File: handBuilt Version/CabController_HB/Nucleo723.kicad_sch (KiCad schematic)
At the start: 13 parts, among them J20 TDU1, J22 CN11, J23 CN12, J24 Screw_Terminal_01x04, J25 CANbus, J26 Battery, J27 SafetyLoop, J29 TDU2, J30 TDU3, J31 TDU4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

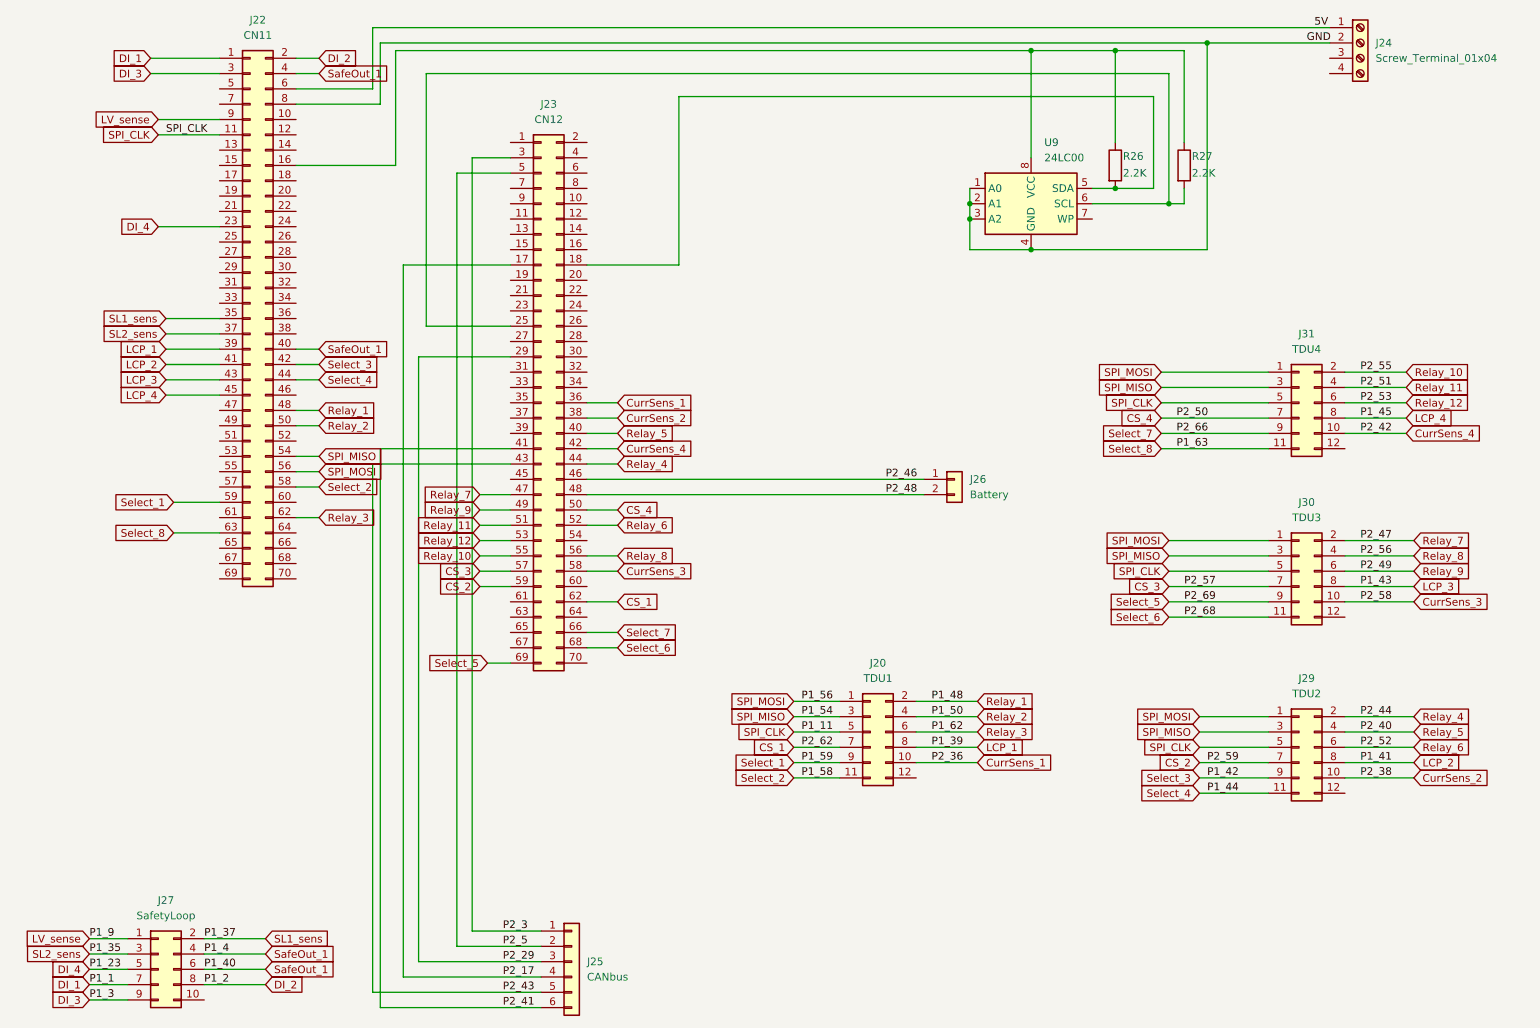
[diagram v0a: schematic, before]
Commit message: changed Connector Pinout for Nucleo
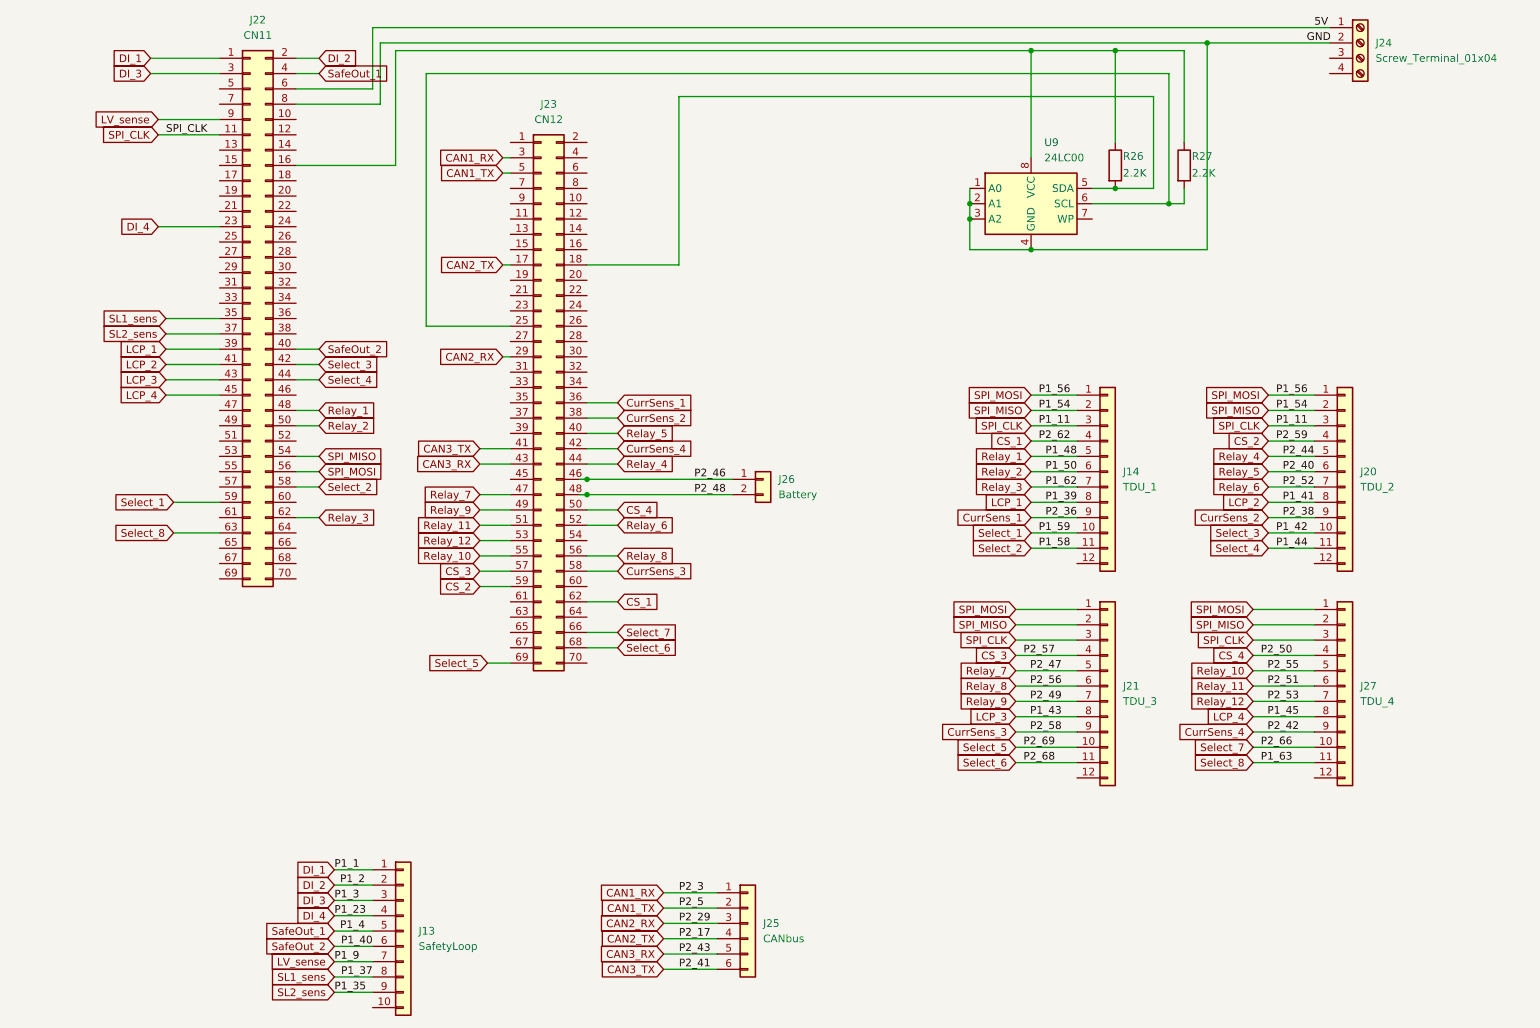
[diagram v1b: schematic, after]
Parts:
- removed J20: TDU1, symbol Connector_Generic:Conn_02x06_Odd_Even
- removed J27: SafetyLoop, symbol Connector_Generic:Conn_02x05_Odd_Even
- removed J29: TDU2, symbol Connector_Generic:Conn_02x06_Odd_Even
- removed J30: TDU3, symbol Connector_Generic:Conn_02x06_Odd_Even
- removed J31: TDU4, symbol Connector_Generic:Conn_02x06_Odd_Even
- added J13: SafetyLoop, symbol Connector_Generic:Conn_01x10
- added J14: TDU_1, symbol Connector_Generic:Conn_01x12
- added J20: TDU_2, symbol Connector_Generic:Conn_01x12
- added J21: TDU_3, symbol Connector_Generic:Conn_01x12
- added J27: TDU_4, symbol Connector_Generic:Conn_01x12
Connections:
- net CS_1: now also J14.4 (Pin_4)
- net CS_2: now also J20.4 (Pin_4)
- net CS_3: now also J21.4 (Pin_4)
- net CS_4: now also J27.4 (Pin_4)
- net CurrSens_1: now also J14.9 (Pin_9)
- net CurrSens_2: now also J20.9 (Pin_9)
- net CurrSens_3: now also J21.9 (Pin_9)
- net CurrSens_4: now also J27.9 (Pin_9)
- net DI_1: now also J13.1 (Pin_1)
- net DI_2: now also J13.2 (Pin_2)
- net DI_3: now also J13.3 (Pin_3)
- net DI_4: now also J13.4 (Pin_4)
- net LCP_1: now also J14.8 (Pin_8)
- net LCP_2: now also J20.8 (Pin_8)
- net LCP_3: now also J21.8 (Pin_8)
- net LCP_4: now also J27.8 (Pin_8)
- net LV_sense: now also J13.7 (Pin_7)
- net Relay_1: now also J14.5 (Pin_5)
- net Relay_10: now also J27.5 (Pin_5)
- net Relay_11: now also J27.6 (Pin_6)
- net Relay_12: now also J27.7 (Pin_7)
- net Relay_2: now also J14.6 (Pin_6)
- net Relay_3: now also J14.7 (Pin_7)
- net Relay_4: now also J20.5 (Pin_5)
- net Relay_5: now also J20.6 (Pin_6)
- net Relay_6: now also J20.7 (Pin_7)
- net Relay_7: now also J21.5 (Pin_5)
- net Relay_8: now also J21.6 (Pin_6)
- net Relay_9: now also J21.7 (Pin_7)
- net SL1_sens: now also J13.8 (Pin_8)
- net SL2_sens: now also J13.9 (Pin_9)
- net SPI_CLK: now also J14.3 (Pin_3), J20.3 (Pin_3), J21.3 (Pin_3), J27.3 (Pin_3)
- net SPI_MISO: now also J14.2 (Pin_2), J20.2 (Pin_2), J21.2 (Pin_2), J27.2 (Pin_2)
- net SPI_MOSI: now also J14.1 (Pin_1), J20.1 (Pin_1), J21.1 (Pin_1), J27.1 (Pin_1)
- net SafeOut_1: now also J13.5 (Pin_5); no longer J22.40 (Pin_40)
- net Select_1: now also J14.10 (Pin_10)
- net Select_2: now also J14.11 (Pin_11)
- net Select_3: now also J20.10 (Pin_10)
- net Select_4: now also J20.11 (Pin_11)
- net Select_5: now also J21.10 (Pin_10)
- net Select_6: now also J21.11 (Pin_11)
- net Select_7: now also J27.10 (Pin_10)
- net Select_8: now also J27.11 (Pin_11)
- net P2_17 renamed CAN2_TX
- net P2_29 renamed CAN2_RX
- net P2_3 renamed CAN1_RX
- net P2_41 renamed CAN3_TX
- net P2_43 renamed CAN3_RX
- net P2_5 renamed CAN1_TX
- new net SafeOut_2: J13.6 (Pin_6), J22.40 (Pin_40)
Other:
- moved on the sheet: J25, J26
